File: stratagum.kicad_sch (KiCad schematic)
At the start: 0 parts

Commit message: Placing symbols for 4-key pad.
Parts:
- added SW1, SW2, SW3, SW4: SW_Push, symbol Switch:SW_Push
- added U1: RP2040 Zero, keyboard_parts:RP2040 Zero (Through Hole), symbol keyboard_parts:RP2040_Zero
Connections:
- new net GND: SW1.1, SW2.1, SW3.1, SW4.1, U1.31 (GND)
- new net key1: SW1.2, U1.0 (GP0)
- new net key2: SW2.2, U1.1 (GP1)
- new net key3: SW3.2, U1.2 (GP2)
- new net key4: SW4.2, U1.3 (GP3)
- no-connect marks 0 -> 18

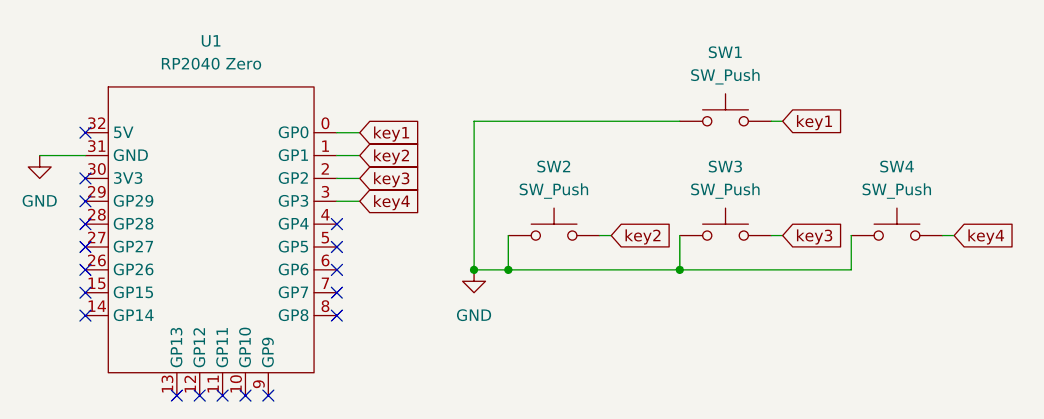
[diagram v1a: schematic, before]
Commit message: Footprints placed for controller and key switches.
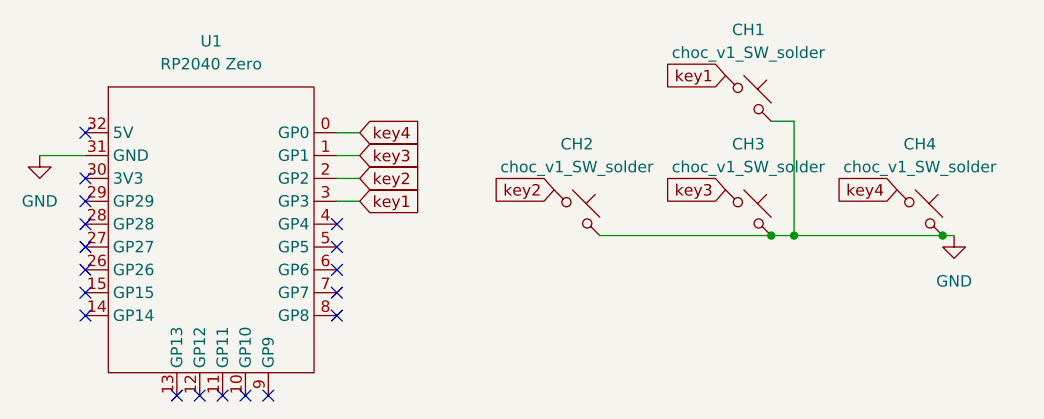
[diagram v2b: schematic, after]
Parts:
- removed SW1, SW2, SW3, SW4: SW_Push, symbol Switch:SW_Push
- added CH1, CH2, CH3, CH4: choc_v1_SW_solder, PCM_marbastlib-xp-choc:SW_choc_v2_1u, symbol PCM_marbastlib-choc:choc_v1_SW_solder
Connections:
- net GND: now also CH1.2, CH2.2, CH3.2, CH4.2
- net key1: now also U1.3 (GP3), CH1.1; no longer U1.0 (GP0)
- net key2: now also U1.2 (GP2), CH2.1; no longer U1.1 (GP1)
- net key3: now also U1.1 (GP1), CH3.1; no longer U1.2 (GP2)
- net key4: now also U1.0 (GP0), CH4.1; no longer U1.3 (GP3)
